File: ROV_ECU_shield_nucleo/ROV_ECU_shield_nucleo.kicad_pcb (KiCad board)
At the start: 4 copper layers, 70.4 x 139.4 mm, 119 parts, among them IC1 DCL541A01, IC2 DCL541A01, IC3 DCL541A01, IC4 DCL541A01, IC5 DCL541A01, IC6 DCL541A01, IC7 ADUM3190TRQZ, IC8 ADUM3190TRQZ, IC9 DCL541A01, J1 PWR_IN, J10 ISO_AN2, J11 PWMO_4, J12 PWMO_5, J13 PWMO_6, J14 PWMI_1, J15 PWMI_2, J16 LED1, J17 LED2, J2 RS485_1, J3 RS485_2, J4 RS485_2_TTL, J5 PWMO_1, J6 DIG_IO, J7 PWMO_2, J8 PWMO_3, J9 ISO_AN1, Q1 FDS6898A, U1 AZ1117-3.3, U2 MAX3485, U3 MAX3485, U4 NUCLEOH723ZG, U5 MAX3485

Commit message: 下記設計方針を定義．設計に反映． ・秋月電子での入手性を優先．（ZHコネクタ，LDO等） ・IMUは6軸（MPU6500は新規非推奨だが量産active） ・IMUメイン用途はレート制御・サブ用途が姿勢制御 ・2次側3.3V生成方法はひとまず秋月の高耐圧LDOとする．
設計TODO：
・ヒューズパッケージ未決定．
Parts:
- removed U1: AZ1117-3.3, Package_TO_SOT_SMD:SOT-223
- added C32: 2.2u, Capacitor_SMD:C_0603_1608Metric_Pad1.08x0.95mm_HandSolder, F.Cu at (6.97, 0.76)
- added C33: 0.1u, Capacitor_SMD:C_0603_1608Metric_Pad1.08x0.95mm_HandSolder, F.Cu at (6.97, 3.27)
- added C34: 0.1u, Capacitor_SMD:C_0603_1608Metric_Pad1.08x0.95mm_HandSolder, F.Cu at (6.97, 5.78)
- added C35: 0.1u, Capacitor_SMD:C_0603_1608Metric_Pad1.08x0.95mm_HandSolder, F.Cu at (6.97, 8.29)
- added C36: 2.2u, Capacitor_SMD:C_0603_1608Metric_Pad1.08x0.95mm_HandSolder, F.Cu at (6.97, 10.8)
- added C37: 0.1u, Capacitor_SMD:C_0603_1608Metric_Pad1.08x0.95mm_HandSolder, F.Cu at (11.3, 0.76)
- added C38: 0.1u, Capacitor_SMD:C_0603_1608Metric_Pad1.08x0.95mm_HandSolder, F.Cu at (11.3, 3.27)
- added C39: 0.1u, Capacitor_SMD:C_0603_1608Metric_Pad1.08x0.95mm_HandSolder, F.Cu at (11.3, 5.78)
- added C40: 2.2u, Capacitor_SMD:C_0603_1608Metric_Pad1.08x0.95mm_HandSolder, F.Cu at (11.3, 8.29)
- added C41: 0.1u, Capacitor_SMD:C_0603_1608Metric_Pad1.08x0.95mm_HandSolder, F.Cu at (11.3, 10.8)
- added C42: 0.1u, Capacitor_SMD:C_0603_1608Metric_Pad1.08x0.95mm_HandSolder, F.Cu at (15.7, 0.76)
- added C43: 0.1u, Capacitor_SMD:C_0603_1608Metric_Pad1.08x0.95mm_HandSolder, F.Cu at (15.7, 3.27)
- added D9: KDZVTR27B, Diode_SMD:D_SOD-123F, F.Cu at (220.0, 64.8)
- added IC10: AP7375-33SA-7, SamacSys_Parts:SOT96P240X110-3N, F.Cu at (1.88, 17.7)
- added IC11: MPU-6500, SamacSys_Parts:QFN40P300X300X95-25N-D, F.Cu at (2.15, 2.15)
- added IC12: MPU-6500, SamacSys_Parts:QFN40P300X300X95-25N-D, F.Cu at (2.15, 7.45)
- added IC13: MPU-6500, SamacSys_Parts:QFN40P300X300X95-25N-D, F.Cu at (2.15, 12.8)
- added J18: GPIO_2, Connector_JST:JST_ZH_B6B-ZR_1x06_P1.50mm_Vertical, F.Cu at (7.33, 14.4)
- added R45: 4.7k, Resistor_SMD:R_0603_1608Metric_Pad0.98x0.95mm_HandSolder, F.Cu at (15.7, 10.8)
- C2: value 22u -> 1u
- C24, C29: value 0.1u -> TBD
- C3: value 22u -> 10u
- J6: value DIG_IO -> GPIO_1; footprint Connector_JST:JST_ZH_B8B-ZR_1x08_P1.50mm_Vertical -> Connector_JST:JST_ZH_B6B-ZR_1x06_P1.50mm_Vertical
- R25, R26, R27, R28, R29, R31, R32, R33, R34, R35: value 4.7k -> TBD
- R30, R36: value 470 -> TBD
- R43, R44: value 20 -> 4.7k
- moved R43 93.8 mm to (15.7, 5.78)
- moved R44 93.8 mm to (15.7, 8.29)
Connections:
- J1 pad 1: +24V -> Net-(J1-Pin_1)
- J6 pad 1: Net-(D7-CH1) -> +3.3VP
- J6 pad 2: Net-(D7-CH2) -> Net-(D7-CH1)
- J6 pad 3: Net-(D7-CH3) -> Net-(D7-CH2)
- J6 pad 4: Net-(D7-CH4) -> Net-(D7-CH3)
- J6 pad 5: Net-(D8-CH1) -> Net-(D7-CH4)
- J6 pad 6: Net-(D8-CH2) -> GNDPWR
- R43 pad 1: +24V -> +3V3
- R43 pad 2: Net-(J17-Pin_1) -> SSLA0
- R44 pad 1: +24V -> +3V3
- R44 pad 2: Net-(J16-Pin_1) -> SSLA0

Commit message: ・kicad ver. 10.05に変更． ・現在の設計でコミット． ・KiCad Routing Toolsプラグインをインストール．
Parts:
- added C44: 1000p, Capacitor_SMD:C_0603_1608Metric_Pad1.08x0.95mm_HandSolder, F.Cu at (115.4, 84.5)
- added D10: D1213A-04S-7, SamacSys_Parts:SOT65P210X110-6N, F.Cu at (198.8, 66.8)
- added J19: UART, Connector_JST:JST_ZH_B4B-ZR_1x04_P1.50mm_Vertical, F.Cu at (199.0, 61.8)
- added L2: L, Inductor_SMD:L_0603_1608Metric_Pad1.05x0.95mm_HandSolder, F.Cu at (115.4, 87.0)
- added R46: 4.7k, Resistor_SMD:R_0603_1608Metric_Pad0.98x0.95mm_HandSolder, F.Cu at (202.8, 67.2)
- J16, J17: footprint Connector_JST:JST_XH_S2B-XH-A-1_1x02_P2.50mm_Horizontal -> Connector_JST:JST_XH_B2B-XH-A_1x02_P2.50mm_Vertical
- moved J18 212.7 mm to (219.5, 29.2), turned to 180 degrees
- moved C28 179.6 mm to (208.8, 130.2), turned to 180 degrees
- moved R33 171.6 mm to (205.2, 130.2), turned to 180 degrees
- moved C29 131.9 mm to (175.5, 95.2)
- moved R30 129.4 mm to (175.5, 90.5), turned to 180 degrees
- moved R36 127.5 mm to (175.5, 96.8), turned to 180 degrees
- moved C23 120.4 mm to (217.5, 130.2), turned to 180 degrees
- moved R41 119.9 mm to (198.5, 35.8), turned to 90 degrees
- moved R42 119.1 mm to (197.0, 35.8), turned to 90 degrees
- moved R27 116.0 mm to (214.0, 130.2), turned to 180 degrees
- moved R39 115.8 mm to (195.5, 35.8), turned to 90 degrees
- moved R40 114.9 mm to (194.0, 35.8), turned to 90 degrees
- moved L1 72.0 mm to (168.2, 62.8), turned to 180 degrees
- moved C4 70.5 mm to (164.2, 64.5), turned to -90 degrees
- moved C24 59.7 mm to (175.5, 89.0)
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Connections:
- net ADC1_INP10 renamed PC0/ADC1_INP10
- net ADC1_INP15 renamed PA3/ADC1_INP15
- net TIM1_CH1 renamed PE9/TIM1_CH1
- net TIM1_CH2 renamed PE11/TIM1_CH2
- net TIM1_CH3 renamed PE13/TIM1_CH3
- net TIM4_CH3 renamed PD14/TIM4_CH3
- net TIM4_CH4 renamed PD15/TIM4_CH4
- net USART1_RX renamed PB7/USART1_RX
- net USART1_TX renamed PB6/USART1_TX
- net USART2_RX renamed PD6/USART2_RX
- net USART2_TX renamed PD5/USART2_TX
- C21 pad 1: +3V3 -> +3.3VA
- C21 pad 2: GND -> GNDA
- C23 pad 1: GND -> GNDA
- C24 pad 2: GND -> GNDA
- C26 pad 1: +3V3 -> +3.3VA
- C26 pad 2: GND -> GNDA
- C28 pad 1: GND -> GNDA
- C29 pad 2: GND -> GNDA
- IC1 pad 4: unconnected-(IC1-VI2-Pad4) -> PE15/D37
- IC11 pad 22: SSLA0 -> PE7/D41
- IC11 pad 23: RSPCKA -> PA5/SPI1_SCK
- IC11 pad 24: MOSIA -> PB5/SPI1_MOSI
- IC11 pad 9: MISOA -> PA6/SPI1_MISO
- IC12 pad 22: SSLA0 -> PE8/D42
- IC12 pad 23: RSPCKA -> PA5/SPI1_SCK
- IC12 pad 24: MOSIA -> PB5/SPI1_MOSI
- IC12 pad 9: MISOA -> PA6/SPI1_MISO
- IC13 pad 22: SSLA0 -> PG2/D49
- IC13 pad 23: RSPCKA -> PA5/SPI1_SCK
- IC13 pad 24: MOSIA -> PB5/SPI1_MOSI
- IC13 pad 9: MISOA -> PA6/SPI1_MISO
- IC2 pad 4: unconnected-(IC2-VI2-Pad4) -> PE12/D39
- IC2 pad 5: unconnected-(IC2-VI3-Pad5) -> PE10/D40
- IC4 pad 3: unconnected-(IC4-VI1-Pad3) -> PG12/TIM23_CH1
- IC4 pad 4: unconnected-(IC4-VI2-Pad4) -> PF7/TIM23_CH2
- IC4 pad 5: unconnected-(IC4-VI3-Pad5) -> PG14/TIM23_CH3
- IC4 pad 6: unconnected-(IC4-VO4-Pad6) -> PE6/TIM15_CH2
- IC5 pad 3: TIM1_CH4 -> PA0/TIM2_CH1
- IC5 pad 4: TIM2_CH1 -> PB10/TIM2_CH3
- IC5 pad 5: TIM2_CH3 -> PB11/TIM2_CH4
- IC6 pad 3: unconnected-(IC6-VI1-Pad3) -> PF3/TIM23_CH4
- IC6 pad 4: unconnected-(IC6-VI2-Pad4) -> PF9/TIM14_CH1
- IC6 pad 5: unconnected-(IC6-VI3-Pad5) -> PD1/D66/FDCAN1_TX
- IC6 pad 6: unconnected-(IC6-VO4-Pad6) -> PD0/D67/FDCAN1_RX
- IC7 pad 1: +3V3 -> +3.3VA
- IC7 pad 2: GND -> GNDA
- IC7 pad 8: GND -> GNDA
- IC8 pad 1: +3V3 -> +3.3VA
- IC8 pad 2: GND -> GNDA
- IC8 pad 8: GND -> GNDA
- IC9 pad 3: unconnected-(IC9-VI1-Pad3) -> PC8/TIM3_CH3
- IC9 pad 4: unconnected-(IC9-VI2-Pad4) -> PC9/TIM3_CH4
- R27 pad 2: +3V3 -> +3.3VA
- R33 pad 2: +3V3 -> +3.3VA
- R39 pad 1: Net-(IC9-VO2) -> Net-(IC9-VO1)
- R41 pad 1: Net-(IC9-VO1) -> Net-(IC9-VO2)
- R43 pad 2: SSLA0 -> PE7/D41
- R44 pad 2: SSLA0 -> PE8/D42
- R45 pad 2: SSLA0 -> PG2/D49
- U4 pad CN10_1: unconnected-(U4F-AVDD-PadCN10_1) -> Net-(U4F-AVDD)
- U4 pad CN10_12: unconnected-(U4F-D2/IO-PadCN10_12) -> PG14/TIM23_CH3
- U4 pad CN10_17: unconnected-(U4F-GND_CN10__1-PadCN10_17) -> GND
- U4 pad CN10_18: unconnected-(U4F-D42/TIMER_A_PWM1N-PadCN10_18) -> PE8/D42
- U4 pad CN10_2: unconnected-(U4F-D7/IO-PadCN10_2) -> PG12/TIM23_CH1
- U4 pad CN10_20: unconnected-(U4F-D41/TIMER_A_ETR-PadCN10_20) -> PE7/D41
- U4 pad CN10_22: unconnected-(U4F-GND_CN10__2-PadCN10_22) -> GND
- U4 pad CN10_24: unconnected-(U4F-D40/TIMER_A_PWM2N-PadCN10_24) -> PE10/D40
- U4 pad CN10_26: unconnected-(U4F-D39/TIMER_A_PWM3N-PadCN10_26) -> PE12/D39
- U4 pad CN10_27: unconnected-(U4F-GND_CN10__3-PadCN10_27) -> GND
- U4 pad CN10_28: unconnected-(U4F-D38/TIMER_A_BKIN2-PadCN10_28) -> PE6/TIM15_CH2
- U4 pad CN10_29: TIM2_CH1 -> PA0/TIM2_CH1
- U4 pad CN10_3: unconnected-(U4F-AGND_CN10-PadCN10_3) -> GNDA
- U4 pad CN10_30: unconnected-(U4F-D37/TIMER_A_BKIN1-PadCN10_30) -> PE15/D37
- U4 pad CN10_32: TIM2_CH3 -> PB10/TIM2_CH3
- U4 pad CN10_34: TIM2_CH4 -> PB11/TIM2_CH4
- U4 pad CN10_5: unconnected-(U4F-GND_CN10-PadCN10_5) -> GND
- U4 pad CN10_8: TIM1_CH4 -> PE14/TIM1_CH4
- U4 pad CN7_1: unconnected-(U4E-D16/I2S_A_MCK-PadCN7_1) -> PC6/USART6_TX
- U4 pad CN7_10: SPI1_SCK -> PA5/SPI1_SCK
- U4 pad CN7_11: unconnected-(U4E-D21/I2S_B_MCK-PadCN7_11) -> PC7/USART6_RX
- U4 pad CN7_12: SPI1_MISO -> PA6/SPI1_MISO
- U4 pad CN7_14: SPI1_MOSI -> PB5/SPI1_MOSI
- U4 pad CN7_20: unconnected-(U4E-D8/IO-PadCN7_20) -> PF3/TIM23_CH4
- U4 pad CN7_8: unconnected-(U4E-GND_CN7-PadCN7_8) -> GND
- U4 pad CN8_11: unconnected-(U4C-GND_CN8-PadCN8_11) -> GND
- U4 pad CN8_13: unconnected-(U4C-GND_CN8__1-PadCN8_13) -> GND
- U4 pad CN8_14: unconnected-(U4C-D49/IO-PadCN8_14) -> PG2/D49
- U4 pad CN8_16: unconnected-(U4C-D50/IO-PadCN8_16) -> PG3/D50
- U4 pad CN8_2: unconnected-(U4C-D43/SDMMC_D0-PadCN8_2) -> PC8/TIM3_CH3
- U4 pad CN8_4: unconnected-(U4C-D44/SDMMC_D1/I2S_A_CKIN-PadCN8_4) -> PC9/TIM3_CH4
- U4 pad CN8_9: +5V -> unconnected-(U4C-5V_CN8-PadCN8_9)
- U4 pad CN9_11: ADC3_INP6 -> unconnected-(U4D-A5/ADC3_INP6/I2C1_SCL-PadCN9_11)
- U4 pad CN9_12: unconnected-(U4D-GND_CN9-PadCN9_12) -> GND
- U4 pad CN9_23: unconnected-(U4D-GND_CN9__1-PadCN9_23) -> GND
- U4 pad CN9_25: unconnected-(U4D-D67/CAN_RX-PadCN9_25) -> PD0/D67/FDCAN1_RX
- U4 pad CN9_26: unconnected-(U4D-D62/SAI_B_MCLK-PadCN9_26) -> PF7/TIM23_CH2
- U4 pad CN9_27: unconnected-(U4D-D66/CAN_TX-PadCN9_27) -> PD1/D66/FDCAN1_TX
- U4 pad CN9_28: unconnected-(U4D-D63/SAI_B_FS-PadCN9_28) -> PF9/TIM14_CH1
- U4 pad CN9_29: unconnected-(U4D-D65/IO-PadCN9_29) -> PG0/D65
- U4 pad CN9_30: unconnected-(U4D-D64/IO-PadCN9_30) -> PG1/D64
- U4 pad CN9_5: ADC3_INP1 -> unconnected-(U4D-A2/ADC12_INP13-PadCN9_5)
- U4 pad CN9_7: ADC1_INP5 -> unconnected-(U4D-A3/ADC12_INP5-PadCN9_7)
- U4 pad CN9_9: ADC3_INP0 -> unconnected-(U4D-A4/ADC123_INP12/I2C1_SDA-PadCN9_9)
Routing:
- net +3.3VP: track 20.1 -> 161.6 mm, vias 1 -> 12
- net PD1/D66/FDCAN1_TX: track 0.00 -> 121.0 mm, vias 0 -> 1
- net PF9/TIM14_CH1: track 0.00 -> 112.2 mm, vias 0 -> 2
- net PD0/D67/FDCAN1_RX: track 0.00 -> 111.5 mm, vias 0 -> 1
- net PF7/TIM23_CH2: track 0.00 -> 84.1 mm
- net PE6/TIM15_CH2: track 0.00 -> 81.7 mm, vias 0 -> 2
- net PD15/TIM4_CH4: track 0.00 -> 72.7 mm, vias 0 -> 1
- net PE10/D40: track 0.00 -> 68.3 mm, vias 0 -> 1
- net PD14/TIM4_CH3: track 0.00 -> 65.1 mm, vias 0 -> 2
- net PE12/D39: track 0.00 -> 64.6 mm, vias 0 -> 1
- net PB7/USART1_RX: track 0.00 -> 63.2 mm, vias 0 -> 1
- net PB6/USART1_TX: track 0.00 -> 62.4 mm, vias 0 -> 1
- net Net-(IC7-EAOUT): track 0.00 -> 58.9 mm, vias 0 -> 2
- net PG14/TIM23_CH3: track 0.00 -> 56.3 mm, vias 0 -> 1
- net GNDPWR: track 13.4 -> 68.8 mm, vias 0 -> 3
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
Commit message: 更新
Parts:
- removed R19: 120, Resistor_SMD:R_0603_1608Metric_Pad0.98x0.95mm_HandSolder
- removed R20: 10, Resistor_SMD:R_0603_1608Metric_Pad0.98x0.95mm_HandSolder
- removed R21: 1k, Resistor_SMD:R_0603_1608Metric_Pad0.98x0.95mm_HandSolder
- removed R22, R23, R24: 4.7k, Resistor_SMD:R_0603_1608Metric_Pad0.98x0.95mm_HandSolder
- removed U5: MAX3485, Package_SO:SOIC-8_3.9x4.9mm_P1.27mm
- added AC1: BNO085, SamacSys_Parts:BNO085, F.Cu at (131.2, 111.2)
- added C45: 0.1u, Capacitor_SMD:C_0603_1608Metric_Pad1.08x0.95mm_HandSolder, F.Cu at (129.5, 32.8)
- added C46: 0.1u, Capacitor_SMD:C_0603_1608Metric_Pad1.08x0.95mm_HandSolder, F.Cu at (138.0, 34.0)
- added C47: 0.1u, Capacitor_SMD:C_0603_1608Metric_Pad1.08x0.95mm_HandSolder, F.Cu at (138.0, 37.5)
- added C48: 10u, Capacitor_SMD:C_0603_1608Metric_Pad1.08x0.95mm_HandSolder, F.Cu at (100.1, 73.8)
- added D11: D, Diode_SMD:D_SOD-323_HandSoldering, F.Cu at (103.0, 76.2)
- added F3: 20A, Fuse:Fuseholder_Blade_Mini_Keystone_3568, F.Cu at (99.0, 108.8)
- added IC14: ATA6561-GAQW-N, SamacSys_Parts:SOIC127P600X175-8N, F.Cu at (134.5, 35.8)
- added IC15: AP7375-50SA-7, SamacSys_Parts:SOT96P240X110-3N, F.Cu at (100.0, 76.2)
- added J20: I2C, Connector_JST:JST_ZH_B4B-ZR_1x04_P1.50mm_Vertical, F.Cu at (138.8, 64.5)
- added J21: 3.3VPO, Connector_JST:JST_ZH_B2B-ZR_1x02_P1.50mm_Vertical, F.Cu at (111.0, 159.2)
- added R47: 4.7k, Resistor_SMD:R_0603_1608Metric_Pad0.98x0.95mm_HandSolder, F.Cu at (159.8, 119.0)
- added R48: 4.7k, Resistor_SMD:R_0603_1608Metric_Pad0.98x0.95mm_HandSolder, F.Cu at (159.8, 102.8)
- added R49: 4.7k, Resistor_SMD:R_0603_1608Metric_Pad0.98x0.95mm_HandSolder, F.Cu at (148.0, 81.5)
- added R50: 4.7k, Resistor_SMD:R_0603_1608Metric_Pad0.98x0.95mm_HandSolder, F.Cu at (148.0, 78.8)
- added R51: 4.7k, Resistor_SMD:R_0603_1608Metric_Pad0.98x0.95mm_HandSolder, F.Cu at (115.9, 99.0)
- added R52: 4.7k, Resistor_SMD:R_0603_1608Metric_Pad0.98x0.95mm_HandSolder, F.Cu at (159.8, 105.8)
- added R53: 4.7k, Resistor_SMD:R_0603_1608Metric_Pad0.98x0.95mm_HandSolder, F.Cu at (116.2, 67.4)
- added R54: 4.7k, Resistor_SMD:R_0603_1608Metric_Pad0.98x0.95mm_HandSolder, F.Cu at (116.2, 68.9)
- C11: value 0.1u -> 1u
- C44: value 1000p -> 0.1u
- J1: value PWR_IN -> 24VPI; footprint Connector_JST:JST_XH_S2B-XH-A-1_1x02_P2.50mm_Horizontal -> Connector_JST:JST_ZH_B2B-ZR_1x02_P1.50mm_Vertical
- J16: value LED1 -> NMOS_SW1; footprint Connector_JST:JST_XH_B2B-XH-A_1x02_P2.50mm_Vertical -> Connector_JST:JST_ZH_B2B-ZR_1x02_P1.50mm_Vertical
- J17: value LED2 -> NMOS_SW2; footprint Connector_JST:JST_XH_B2B-XH-A_1x02_P2.50mm_Vertical -> Connector_JST:JST_ZH_B2B-ZR_1x02_P1.50mm_Vertical
- J4: value RS485_2_TTL -> CAN
- R17: value 1k -> 60
- R18: value 10 -> 60
- moved R43 178.7 mm to (159.8, 111.5), turned to 180 degrees
- moved R44 175.5 mm to (159.8, 108.5), turned to 180 degrees
- moved IC13 173.8 mm to (141.2, 116.9)
- moved C42 173.1 mm to (140.4, 120.8), turned to -90 degrees
- moved C43 172.9 mm to (142.5, 120.8), turned to -90 degrees
- moved C41 172.3 mm to (144.0, 120.8), turned to -90 degrees
- moved C40 170.0 mm to (138.8, 120.8), turned to -90 degrees
- moved C37 164.2 mm to (123.4, 120.8), turned to -90 degrees
- moved IC12 161.7 mm to (121.2, 116.9)
- moved IC11 161.7 mm to (131.2, 99.6)
- moved C33 161.3 mm to (133.4, 103.5), turned to -90 degrees
- moved C38 160.3 mm to (120.4, 120.8), turned to -90 degrees
- moved C39 159.5 mm to (121.9, 120.8), turned to -90 degrees
- moved C32 159.4 mm to (128.9, 103.5), turned to -90 degrees
- moved R16 158.4 mm to (99.5, 146.8), turned to -90 degrees
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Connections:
- net Net-(D8-CH2) renamed CANBUS_STBY
- net Net-(D8-CH3) renamed CANBUS_TX
- net Net-(D8-CH4) renamed CANBUS_RX
- C11 pad 1: +3.3VP -> +24V
- D10 pad 1: unconnected-(D10-CH1-Pad1) -> PB9/I2C1_SDA
- D10 pad 3: unconnected-(D10-CH2-Pad3) -> PB8/I2C1_SCL
- D3 pad 1: unconnected-(D3-CH1-Pad1) -> Net-(D3-CH1)
- D3 pad 3: unconnected-(D3-CH2-Pad3) -> Net-(D3-CH2)
- D3 pad 4: Net-(D3-CH3) -> unconnected-(D3-CH3-Pad4)
- D3 pad 5: +3.3VP -> +5VP
- D3 pad 6: Net-(D3-CH4) -> unconnected-(D3-CH4-Pad6)
- IC12 pad 23: PA5/SPI1_SCK -> PD3/SPI2_SCK
- IC12 pad 24: PB5/SPI1_MOSI -> PC3/SPI2_MOSI
- IC12 pad 9: PA6/SPI1_MISO -> PC2/SPI2_MISO
- IC13 pad 23: PA5/SPI1_SCK -> PB3/SPI3_SCK
- IC13 pad 24: PB5/SPI1_MOSI -> PC12/SPI3_MOSI
- IC13 pad 9: PA6/SPI1_MISO -> PB4/SPI3_MISO
- IC2 pad 12: UART_BUS2_DEV_EN -> unconnected-(IC2-VO3-Pad12)
- IC2 pad 5: PE10/D40 -> unconnected-(IC2-VI3-Pad5)
- J16 pad 1: Net-(J16-Pin_1) -> +24V
- J17 pad 1: Net-(J17-Pin_1) -> +24V
- J4 pad 1: +3.3VP -> +5VP
- J4 pad 2: Net-(D3-CH3) -> Net-(D3-CH2)
- J4 pad 3: Net-(D3-CH4) -> Net-(D3-CH1)
- R17 pad 1: +3.3VP -> Net-(C45-Pad1)
- R17 pad 2: Net-(U5-B) -> Net-(D3-CH1)
- R18 pad 1: Net-(U5-A) -> Net-(D3-CH2)
- R18 pad 2: Net-(D2-CH1) -> Net-(C45-Pad1)
- R39 pad 1: Net-(IC9-VO1) -> Net-(IC9-VO2)
- R41 pad 1: Net-(IC9-VO2) -> Net-(IC9-VO1)
- U4 pad CN10_24: PE10/D40 -> unconnected-(U4F-D40/TIMER_A_PWM2N-PadCN10_24)
- U4 pad CN7_10: PA5/SPI1_SCK -> PB8/I2C1_SCL
- U4 pad CN7_15: unconnected-(U4E-D23/I2S_B_CK/SPI_B_SCK-PadCN7_15) -> PB3/SPI3_SCK
- U4 pad CN7_19: unconnected-(U4E-D25/SPI_B_MISO-PadCN7_19) -> PB4/SPI3_MISO
- U4 pad CN7_2: unconnected-(U4E-D15/I2C_A_SCL-PadCN7_2) -> PA5/SPI1_SCK
- U4 pad CN7_4: unconnected-(U4E-D14/I2C_A_SDA-PadCN7_4) -> PB9/I2C1_SDA
- U4 pad CN8_10: unconnected-(U4C-D47/SDMMC_CK-PadCN8_10) -> PC12/SPI3_MOSI
- U4 pad CN9_5: unconnected-(U4D-A2/ADC12_INP13-PadCN9_5) -> PC3/SPI2_MOSI
- U4 pad CN9_8: unconnected-(U4D-D54/USART_B_RTS-PadCN9_8) -> PD3/SPI2_SCK
- U4 pad CN9_9: unconnected-(U4D-A4/ADC123_INP12/I2C1_SDA-PadCN9_9) -> PC2/SPI2_MISO
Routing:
- net +24V: track 0.00 -> 171.4 mm
- net +3.3VP: track 161.6 -> 268.0 mm
- net +5VP: track 0.00 -> 78.6 mm, vias 0 -> 2
- net +3V3: track 42.0 -> 117.9 mm, vias 4 -> 12
- net PE10/D40: track 68.3 -> 0.00 mm, vias 1 -> 0
- net PC12/SPI3_MOSI: track 0.00 -> 59.2 mm, vias 0 -> 1
- net GNDPWR: track 68.8 -> 127.5 mm, vias 3 -> 2
- net Net-(J1-Pin_1): track 0.00 -> 56.6 mm
- net +3.3VA: track 22.5 -> 76.2 mm, vias 0 -> 3
- net GNDA: track 4.49 -> 52.3 mm, vias 0 -> 2
- net PB3/SPI3_SCK: track 0.00 -> 45.1 mm
- net PWM_IN_1: track 22.7 -> 56.2 mm
- net PWM_IN_2: track 30.1 -> 60.7 mm
- net Net-(D2-CH2): track 36.7 -> 7.37 mm
- net CANBUS_STBY: track 14.9 -> 43.1 mm, vias 2 -> 3
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- added copper zone on F.Cu, net Net-(J16-Pin_2)
- added copper zone on F.Cu, net Net-(J17-Pin_2)
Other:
- board size 70.4 x 139.4 mm -> 70 x 139.4 mm

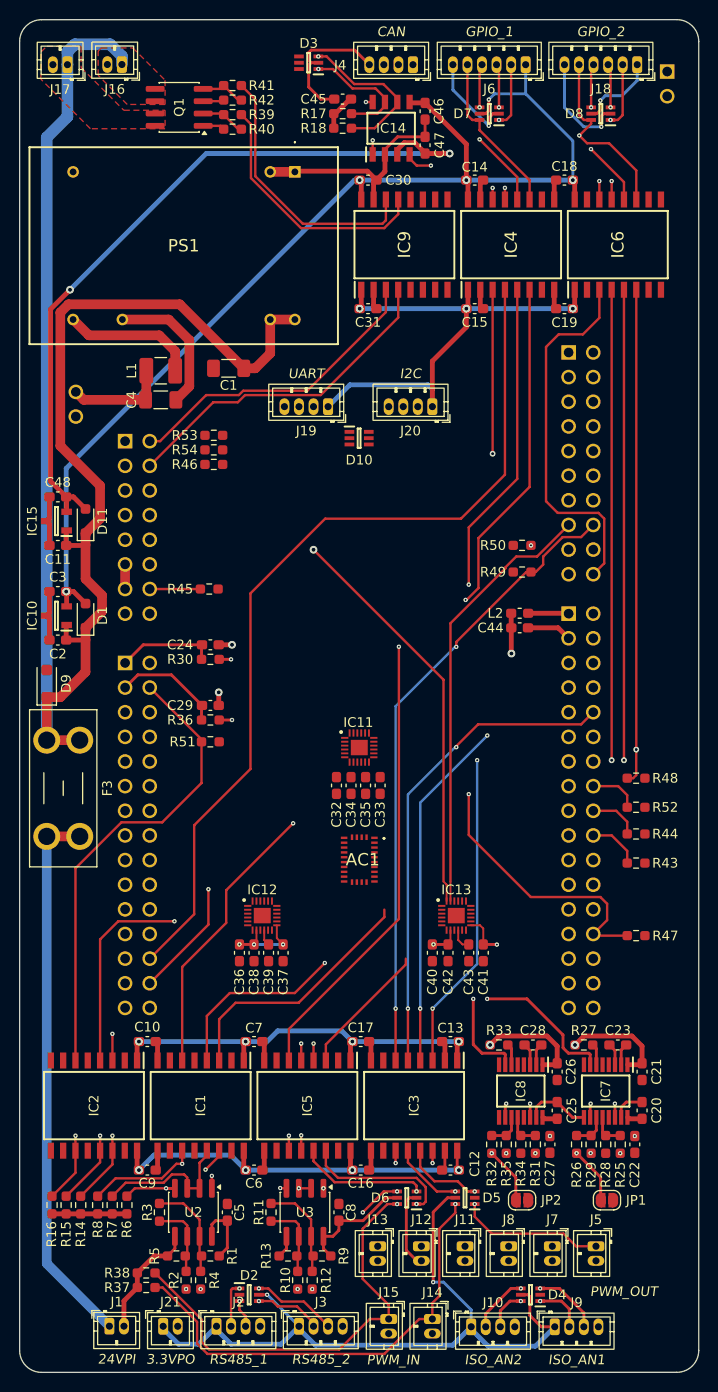
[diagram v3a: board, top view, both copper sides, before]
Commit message: ・sch 誤接続修正（I2C1_SCL/SPI1_SCK）修正． ・BNO085 H_INTN端子を外部割込み端子へ接続． ・A/Wレイアウトブラッシュアップ．
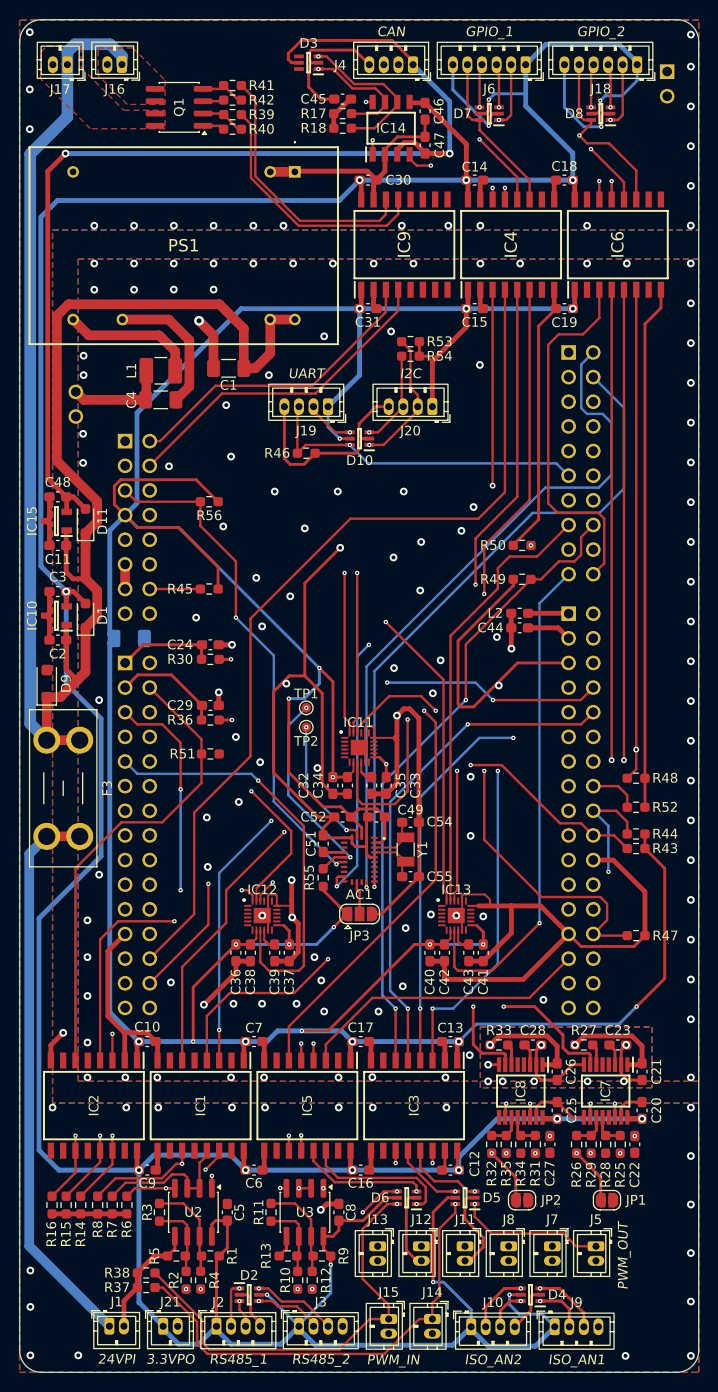
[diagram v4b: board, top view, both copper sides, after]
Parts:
- added C49: 0.1u, Capacitor_SMD:C_0603_1608Metric_Pad1.08x0.95mm_HandSolder, F.Cu at (133.0, 106.8)
- added C50: 4.7u, Capacitor_SMD:C_1206_3216Metric_Pad1.33x1.80mm_HandSolder, B.Cu at (107.5, 88.3)
- added C51: 0.1u, Capacitor_SMD:C_0603_1608Metric_Pad1.08x0.95mm_HandSolder, F.Cu at (127.5, 109.5)
- added C52: 0.1u, Capacitor_SMD:C_0603_1608Metric_Pad1.08x0.95mm_HandSolder, F.Cu at (129.5, 106.8)
- added C54: 22p, Capacitor_SMD:C_0603_1608Metric_Pad1.08x0.95mm_HandSolder, F.Cu at (136.5, 107.3)
- added C55: 22p, Capacitor_SMD:C_0603_1608Metric_Pad1.08x0.95mm_HandSolder, F.Cu at (136.5, 112.9)
- added JP3: SolderJumper_3_Open, Jumper:SolderJumper-3_P1.3mm_Open_RoundedPad1.0x1.5mm, F.Cu at (131.2, 116.8)
- added R55: 10k, Resistor_SMD:R_0603_1608Metric_Pad0.98x0.95mm_HandSolder, F.Cu at (127.5, 113.0)
- added R56: 10k, Resistor_SMD:R_0603_1608Metric_Pad0.98x0.95mm_HandSolder, F.Cu at (115.8, 74.2)
- added TP1: TestPoint, TestPoint:TestPoint_Pad_D1.0mm, F.Cu at (125.8, 95.5)
- added TP2: TestPoint, TestPoint:TestPoint_Pad_D1.0mm, F.Cu at (125.8, 97.5)
- added Y1: 32.768k, Crystal:Crystal_SMD_3215-2Pin_3.2x1.5mm, F.Cu at (136.0, 110.1)
- moved R53 22.5 mm to (136.5, 57.8), turned to 180 degrees
- moved R54 22.5 mm to (136.5, 59.2), turned to 180 degrees
- moved R46 9.60 mm to (125.8, 69.2), turned to 0 degrees
- moved R43 1.50 mm to (159.8, 110.0)
- moved R51 1.25 mm to (115.9, 100.2)
- moved R49 0.75 mm to (148.0, 82.2)
- moved C37 0.63 mm to (124.0, 120.8)
- moved C39 0.63 mm to (122.5, 120.8)
- moved C33 0.63 mm to (134.0, 103.5)
- moved C35 0.63 mm to (132.5, 103.5)
- moved C32 0.37 mm to (128.5, 103.5)
- moved C34 0.37 mm to (130.0, 103.5)
- moved C42 0.37 mm to (140.0, 120.8)
- moved C38 0.37 mm to (120.0, 120.8)
- moved C36 0.37 mm to (118.5, 120.8)
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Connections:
- AC1 pad 10: unconnected-(AC1-CLKSEL0-Pad10) -> Net-(AC1-CLKSEL0)
- AC1 pad 11: unconnected-(AC1-NRST-Pad11) -> nRST
- AC1 pad 14: unconnected-(AC1-H_INTN-Pad14) -> PE14/EXTI14
- AC1 pad 17: unconnected-(AC1-SA0/H_MOSI-Pad17) -> Net-(AC1-SA0/H_MOSI)
- AC1 pad 19: unconnected-(AC1-H_SCL/SCK/RX-Pad19) -> PB8/I2C1_SCL
- AC1 pad 2: unconnected-(AC1-GND_1-Pad2) -> GND
- AC1 pad 20: unconnected-(AC1-H_SDA/H_MISO/TX-Pad20) -> PB9/I2C1_SDA
- AC1 pad 25: unconnected-(AC1-GND_2-Pad25) -> GND
- AC1 pad 26: unconnected-(AC1-XOUT32/CLKSEL1-Pad26) -> Net-(AC1-XOUT32/CLKSEL1)
- AC1 pad 27: unconnected-(AC1-XIN32-Pad27) -> Net-(AC1-XIN32)
- AC1 pad 28: unconnected-(AC1-VDDIO-Pad28) -> +3V3
- AC1 pad 3: unconnected-(AC1-VDD-Pad3) -> +3V3
- AC1 pad 4: unconnected-(AC1-BOOTN-Pad4) -> Net-(AC1-BOOTN)
- AC1 pad 5: unconnected-(AC1-PS1-Pad5) -> GND
- AC1 pad 6: unconnected-(AC1-PS0/WAKE-Pad6) -> GND
- AC1 pad 9: unconnected-(AC1-CAP-Pad9) -> Net-(AC1-CAP)
- U4 pad CN10_8: PE14/TIM1_CH4 -> PE14/EXTI14
- U4 pad CN7_10: PB8/I2C1_SCL -> PA5/SPI1_SCK
- U4 pad CN7_2: PA5/SPI1_SCK -> PB8/I2C1_SCL
- U4 pad CN8_5: unconnected-(U4C-NRST_CN8-PadCN8_5) -> nRST
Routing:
- net GND: track 31.4 -> 458.3 mm, vias 0 -> 113
- net +3V3: track 117.9 -> 410.2 mm, vias 12 -> 20
- net GNDPWR: track 127.5 -> 320.7 mm, vias 2 -> 42
- net +3.3VP: track 268.0 -> 429.9 mm, vias 12 -> 16
- net PB9/I2C1_SDA: track 0.00 -> 109.4 mm, vias 0 -> 2
- net PB8/I2C1_SCL: track 0.00 -> 108.5 mm, vias 0 -> 2
- net PA6/SPI1_MISO: track 0.00 -> 59.1 mm, vias 0 -> 1
- net PB5/SPI1_MOSI: track 0.00 -> 56.8 mm, vias 0 -> 1
- net PE14/EXTI14: track 0.00 -> 55.1 mm, vias 0 -> 4
- net PG2/D49: track 5.22 -> 58.2 mm, vias 0 -> 1
- net nRST: track 0.00 -> 52.3 mm, vias 0 -> 2
- net PB4/SPI3_MISO: track 0.00 -> 52.0 mm, vias 0 -> 1
- net PA5/SPI1_SCK: track 0.00 -> 46.2 mm, vias 0 -> 1
- net PE8/D42: track 5.22 -> 49.8 mm, vias 0 -> 2
- net PC2/SPI2_MISO: track 0.00 -> 44.0 mm, vias 0 -> 1
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- added copper zone on B.Cu, net GND
- added copper zone on F.Cu, net GND
- added copper zone on In1.Cu, net GND
- added copper zone on B.Cu, net GNDA
- added copper zone on F.Cu, net GNDA
- added copper zone on In1.Cu, net GNDA
- added copper zone on In2.Cu, net GNDA
- added copper zone on B.Cu, net GNDPWR
- added copper zone on F.Cu, net GNDPWR
- added copper zone on In1.Cu, net GNDPWR
